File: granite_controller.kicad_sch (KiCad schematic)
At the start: 0 parts

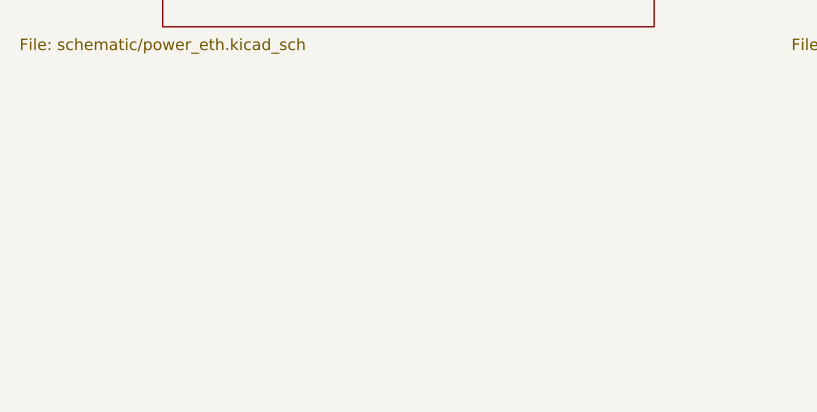
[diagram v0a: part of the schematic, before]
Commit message: Add protected GPIO expansion header
New sheet 'Expansion header' with J8, a 2x18 2.54 mm header (DNP),
bringing out the 28 spare U1 GPIOs plus I2C1, 3V3 and 5V.

- Each signal: 330R series resistor (4x0402 array, MCU side) and a
  TPD4E05U06 ESD clamp at the header pin.
- 3V3 and 5V header pins: PTC fuse plus a TVS to GND.
- PC13-PC15 stay unconnected (backup domain, LSE).
- U1 spare pins labelled GPIO_<pin>; the I2C1 labels on U1 became
  global so the header can reach the bus. Net class patterns added
  for I2C1_*, HDR_3V3 and HDR_5V.
- Board regenerated from the netlist (nothing was placed yet).
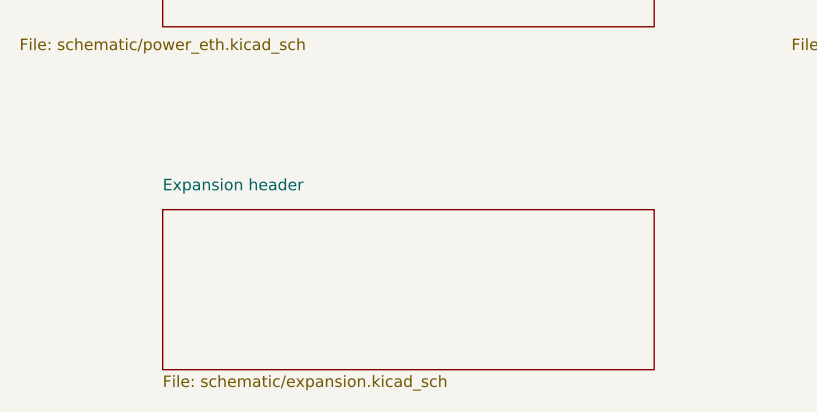
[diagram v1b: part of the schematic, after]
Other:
- added sheet Expansion header (schematic/expansion.kicad_sch)
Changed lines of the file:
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@@
+		)
+	)
+	(sheet
+		(at 31.75 105.41)
+		(size 54.61 17.78)
+		(exclude_from_sim no)
+		(in_bom yes)
+		(on_board yes)
+		(dnp no)
+		(fields_autoplaced yes)
+		(stroke
+			(width 0.1524)
+			(type solid)
+		)
+		(fill
+			(color 0 0 0 0)
+		)
+		(property "Sheetname" "Expansion header"
+			(at 31.75 103.41 0)
+			(show_name no)
+			(do_not_autoplace no)
+			(effects
+				(font
+					(size 1.27 1.27)
+				)
+				(justify left bottom)
+			)
+		)
+		(property "Sheetfile" "schematic/expansion.kicad_sch"
+			(at 31.75 123.78 0)
+			(show_name no)
+			(do_not_autoplace no)
+			(effects
+				(font
+					(size 1.27 1.27)
+				)
+				(justify left top)
+			)
+		)
+		(instances
+			(project "granite_controller"
+				(path "/bd3d1081-8fd5-561e-93ea-9d28b3145149"
+					(page "6")
+				)
+			)
 		)
 	)

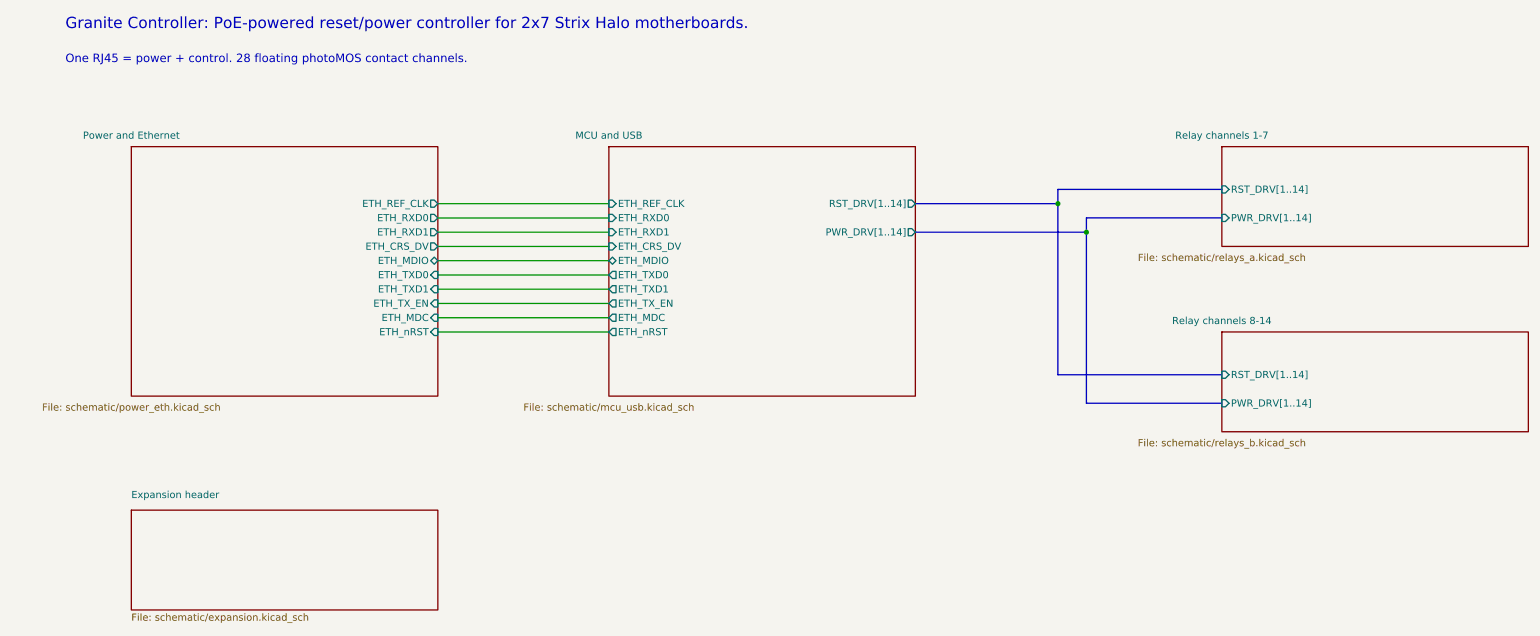
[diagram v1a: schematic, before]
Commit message: Rework for 8 nodes with MCP23017 relay drive
Target is now 8 motherboards per frame (was 14 in the schematic).

- relays_a/relays_b (14 channels, 28 photoMOS) replaced by one
  'Relay channels' sheet: 8 channels, 16 TLP176AM, J11-J18, same
  per-channel circuit and parts.
- U14 MCP23017 @0x20 drives the LEDs: GPA0-7 = PWR_DRV1-8,
  GPB0-7 = RST_DRV1-8. R32 pulls EXP_nRESET low so U14 stays in
  reset (all buttons released) unless the MCU drives it; R33 pulls
  up the shared open-drain EXP_INT.
- MCU: the two 14-bit drive buses are gone; PE2 = EXP_nRESET,
  PE3 = EXP_INT, the other 26 freed pins are no-connect.
- Expansion header J8 grows to 2x20 and carries I2C1, EXP_nRESET
  and EXP_INT (pins 5-8) for extra expander modules or a later
  power board, plus 3V3/5V on both ends.
- Net classes for the second relay bank removed; drive patterns
  point at the new sheet. Board regenerated (nothing placed).
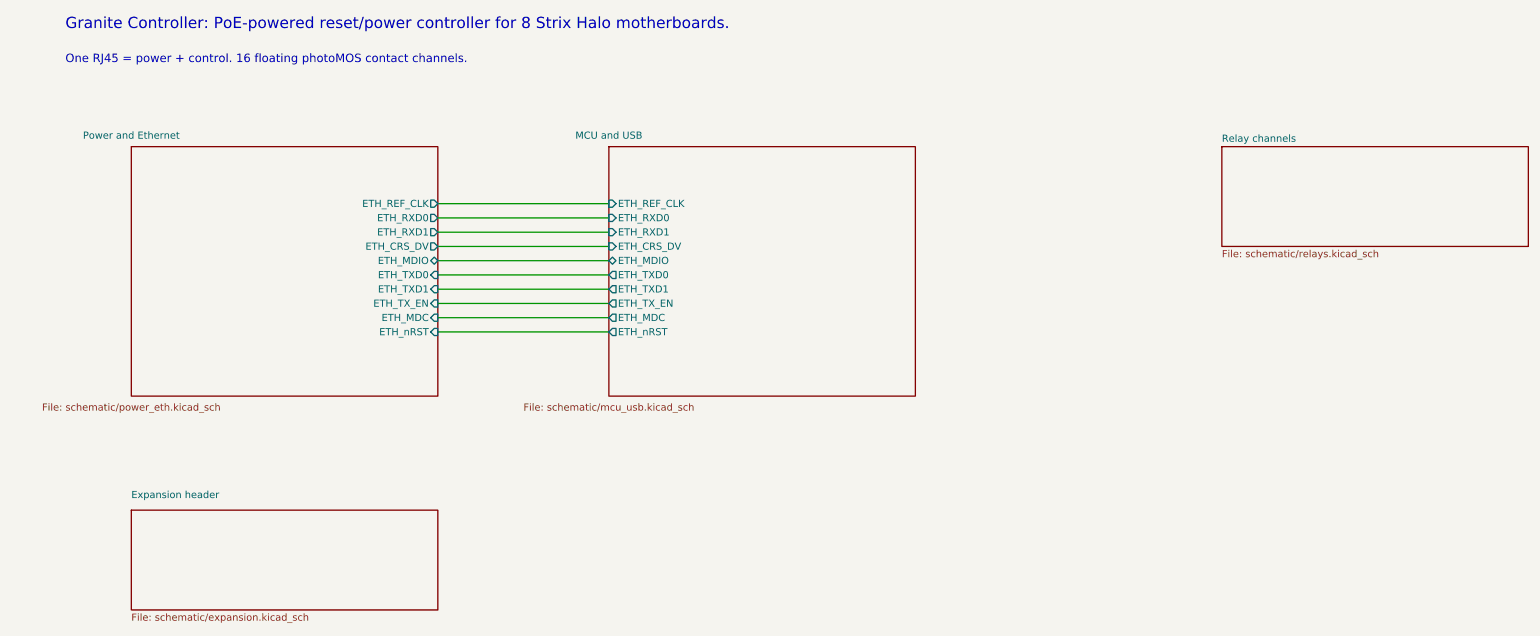
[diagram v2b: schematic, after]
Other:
- removed sheet Relay channels 1-7
- removed sheet Relay channels 8-14
- added sheet Relay channels (schematic/relays.kicad_sch)
- sheet MCU and USB ports: added none; removed PWR_DRV[1..14], RST_DRV[1..14]
- note added: "Granite Controller: PoE-powered reset/power controller for 8 Strix Halo motherboards."
- note added: "One RJ45 = power + control. 16 floating photoMOS contact channels."
- note removed: "Granite Controller: PoE-powered reset/power controller for 2x7 Strix Halo motherboards."
- note removed: "One RJ45 = power + control. 28 floating photoMOS contact channels."

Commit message: Rev C: ESP32-C6 + W5500 controller for immersion
Schematic rework per docs/controller.md.

- MCU: ESP32-C6-MINI-1-N4 replaces STM32H563VIT6 (KiCad-stock
  module). EN/BOOT test pads, USB-C via the C6 USB Serial/JTAG with
  22R series resistors behind the existing USBLC6.
- Ethernet: W5500 over SPI replaces LAN8742A/RMII. PHY network,
  center taps, AVDD ferrite and LED wiring per WIZnet's W5500
  Ethernet Shield reference; ARJP11A magjack and PoE path unchanged.
- I2C split: internal bus (relay MCP23017, TMP1075) on HP I2C with
  its own expander reset (EXP_nRESET_INT, GPIO14); external bus to
  the header (software I2C on GPIO6/7) with EXP_nRESET (GPIO4,
  pulled low) and the shared EXP_INT.
- Expansion header J8 now 2x6: external I2C, reset, interrupt,
  GPIO5/8/15, fused 3V3/5V, all protected as before.
- C1/C2: KEMET T520 molded tantalum-polymer instead of rubber-sealed
  aluminium-polymer cans (immersion).
- Sheets regenerated: Power, Ethernet, MCU replace power_eth and
  mcu_usb; root and project net classes updated (RMII/SWD/RST
  classes removed). Board regenerated, nothing placed yet.
- Spec updated to the captured design.
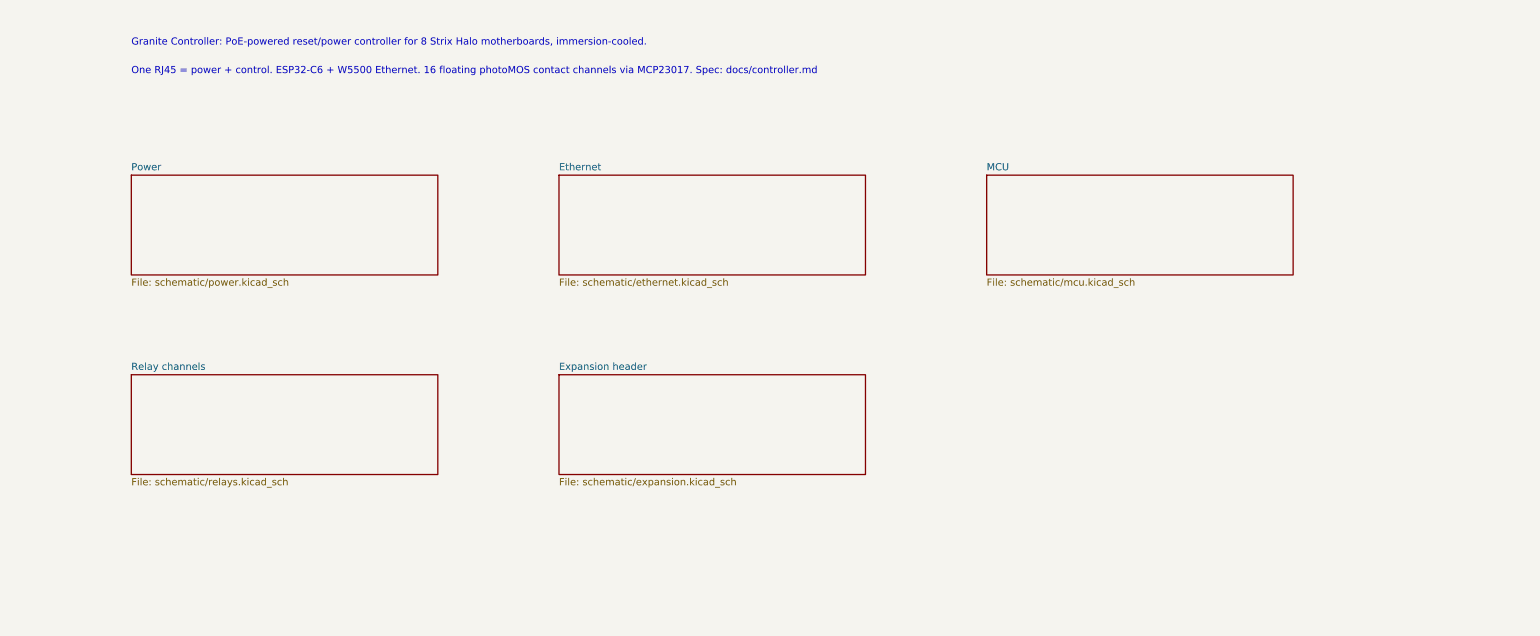
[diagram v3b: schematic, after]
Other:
- removed sheet MCU and USB
- removed sheet Power and Ethernet
- added sheet Ethernet (schematic/ethernet.kicad_sch)
- added sheet MCU (schematic/mcu.kicad_sch)
- added sheet Power (schematic/power.kicad_sch)
- note added: "Granite Controller: PoE-powered reset/power controller for 8 Strix Halo motherboards, immersion-cooled."
- note added: "One RJ45 = power + control. ESP32-C6 + W5500 Ethernet. 16 floating photoMOS contact channels via MCP23017. Spec: docs/controller.md"
- note removed: "Granite Controller: PoE-powered reset/power controller for 8 Strix Halo motherboards."
- note removed: "One RJ45 = power + control. 16 floating photoMOS contact channels."
